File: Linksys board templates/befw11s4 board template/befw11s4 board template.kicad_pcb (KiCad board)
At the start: 2 copper layers, 160 x 138 mm, 46 parts, among them J1 RJ45, J2 RJ45, J3 RJ45, J4 RJ45, J5 RJ45, J6 Barrel_Jack_Switch, J7 switched ground, J8 RJ45, SW2 reset, U1 AMS1117-3.3, U2 AMS1117-5.0, U3 YAAJ_DCDC_StepDown_LM2596

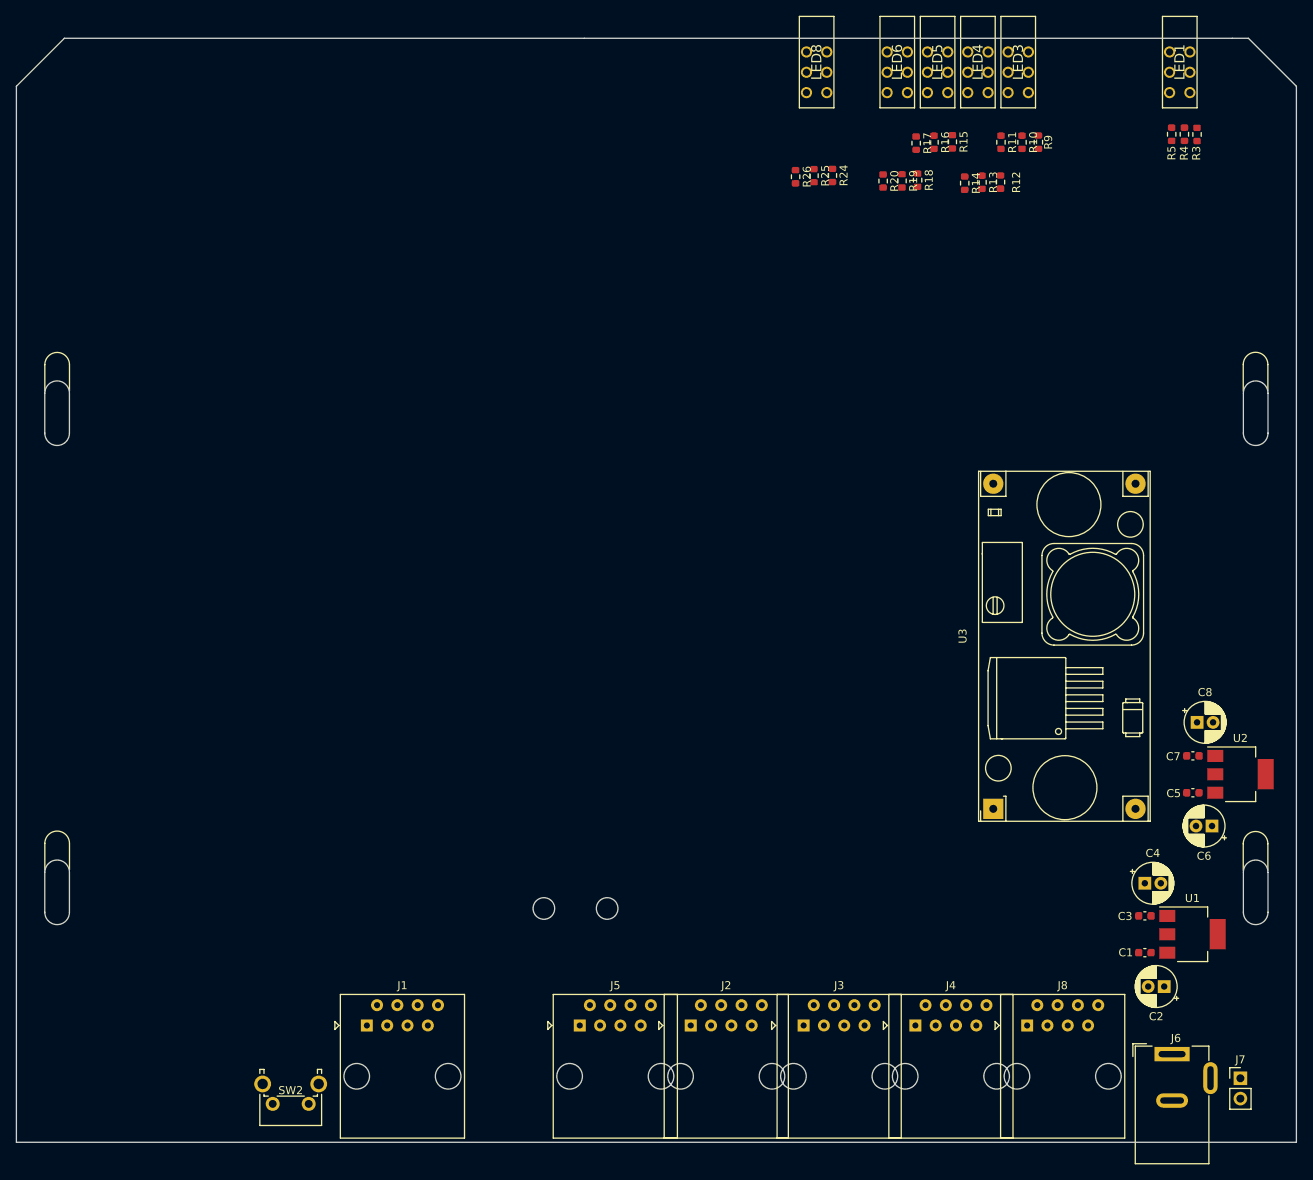
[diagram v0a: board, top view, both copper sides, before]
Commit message: tweaks to locations based on 1:1 printouts
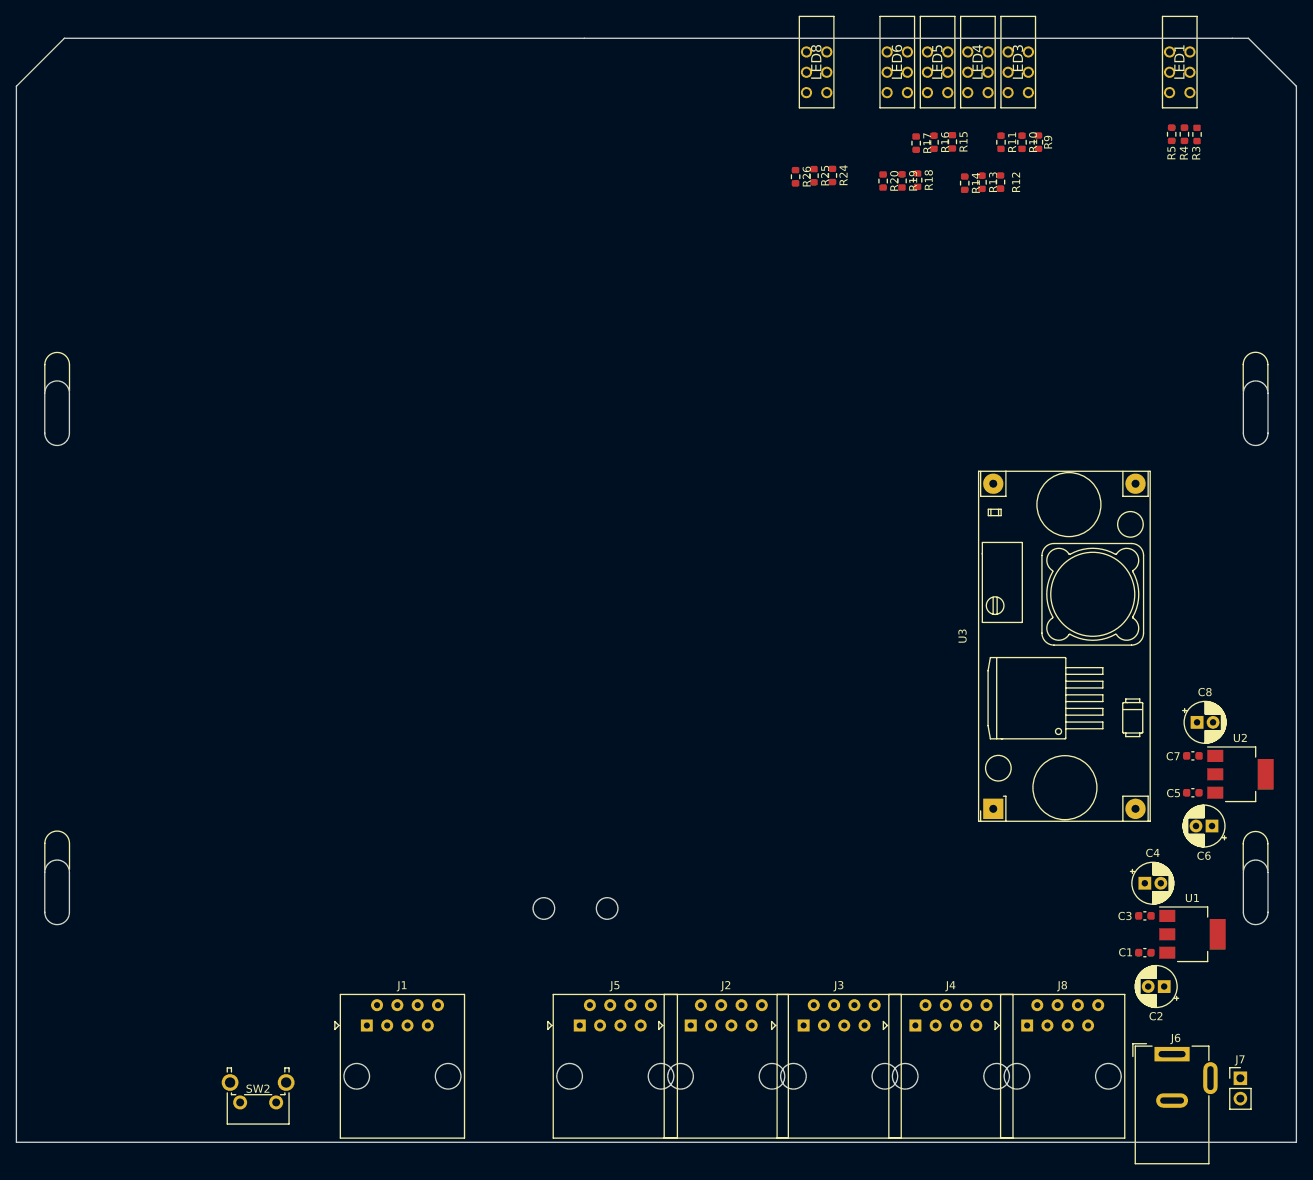
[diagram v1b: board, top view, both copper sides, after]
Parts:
- moved SW2 4.07 mm to (99.5, 155.0)
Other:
- board text removed: "the plunger needs to actually reach 8.2+mm from the edge of the board"
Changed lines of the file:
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@@
   )
   (footprint "Button_Switch_THT:SW_Tactile_SPST_Angled_PTS645Vx58-2LFS" (layer "F.Cu")
-    (at 103.54 155.2 180)
+    (at 99.47 155.02 180)
     (descr "tactile switch SPST right angle, PTS645VL58-2 LFS")
     (tags "tactile switch SPST angled PTS645VL58-2 LFS C&K Button")
@@
   (gr_line (start 220.355001 66.1) (end 220.355001 62.779649) (layer "F.SilkS") (width 0.1))
   (gr_line (start 223.435034 126) (end 223.435034 122.689649) (layer "F.SilkS") (width 0.1))
-  (gr_arc (start 70.555001 62.8) (mid 72.1 61.270345) (end 73.635033 62.81) (layer "F.SilkS") (width 0.1))
+  (gr_arc (start 70.555001 62.8) (mid 72.1 61.270344) (end 73.635033 62.81) (layer "F.SilkS") (width 0.1))
   (gr_line (start 220.355002 126) (end 220.355002 122.679649) (layer "F.SilkS") (width 0.1))
   (gr_line (start 70.555001 66.120351) (end 70.555001 62.8) (layer "F.SilkS") (width 0.1))
-  (gr_arc (start 220.355001 62.779649) (mid 221.9 61.249995) (end 223.435033 62.789649) (layer "F.SilkS") (width 0.1))
+  (gr_arc (start 220.355001 62.779649) (mid 221.9 61.249994) (end 223.435033 62.789649) (layer "F.SilkS") (width 0.1))
   (gr_line (start 73.635033 125.950002) (end 73.635033 122.639651) (layer "F.SilkS") (width 0.1))
   (gr_line (start 73.635033 66.120351) (end 73.635033 62.81) (layer "F.SilkS") (width 0.1))
-  (gr_arc (start 220.355002 122.679649) (mid 221.900001 121.149996) (end 223.435034 122.689649) (layer "F.SilkS") (width 0.1))
+  (gr_arc (start 220.355002 122.679649) (mid 221.900001 121.149995) (end 223.435034 122.689649) (layer "F.SilkS") (width 0.1))
   (gr_line (start 223.435033 66.1) (end 223.435033 62.789649) (layer "F.SilkS") (width 0.1))
-  (gr_arc (start 70.555001 122.629651) (mid 72.1 121.099996) (end 73.635033 122.639651) (layer "F.SilkS") (width 0.1))
+  (gr_arc (start 70.555001 122.629651) (mid 72.1 121.099995) (end 73.635033 122.639651) (layer "F.SilkS") (width 0.1))
   (gr_line (start 70.555001 125.950002) (end 70.555001 122.629651) (layer "F.SilkS") (width 0.1))
   (gr_line (start 227.6 123.8) (end 222.4 123.7) (layer "Cmts.User") (width 0.15))
@@
   (gr_line (start 70.55 71.359976) (end 70.55 66.359976) (layer "Edge.Cuts") (width 0.1))
   (gr_line (start 73 22) (end 138 22) (layer "Edge.Cuts") (width 0.1))
-  (gr_text "the plunger needs to actually reach 8.2+mm \nfrom the edge of the board" (at 235 21) (layer "Cmts.User")
-    (effects (font (size 1 1) (thickness 0.15)))
-  )
   (gr_text "Keep out of these areas so the board mounts to the base" (at 250.5 123.8) (layer "Cmts.User")
     (effects (font (size 1 1) (thickness 0.15)))
